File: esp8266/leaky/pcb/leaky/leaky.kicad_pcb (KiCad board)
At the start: 2 copper layers, 100 x 100 mm, 31 parts, among them J1 UART, J2 extra pins, Q1 BC327, SW1 sensing loop, U1 DD0405MA, U2 ESP-12F

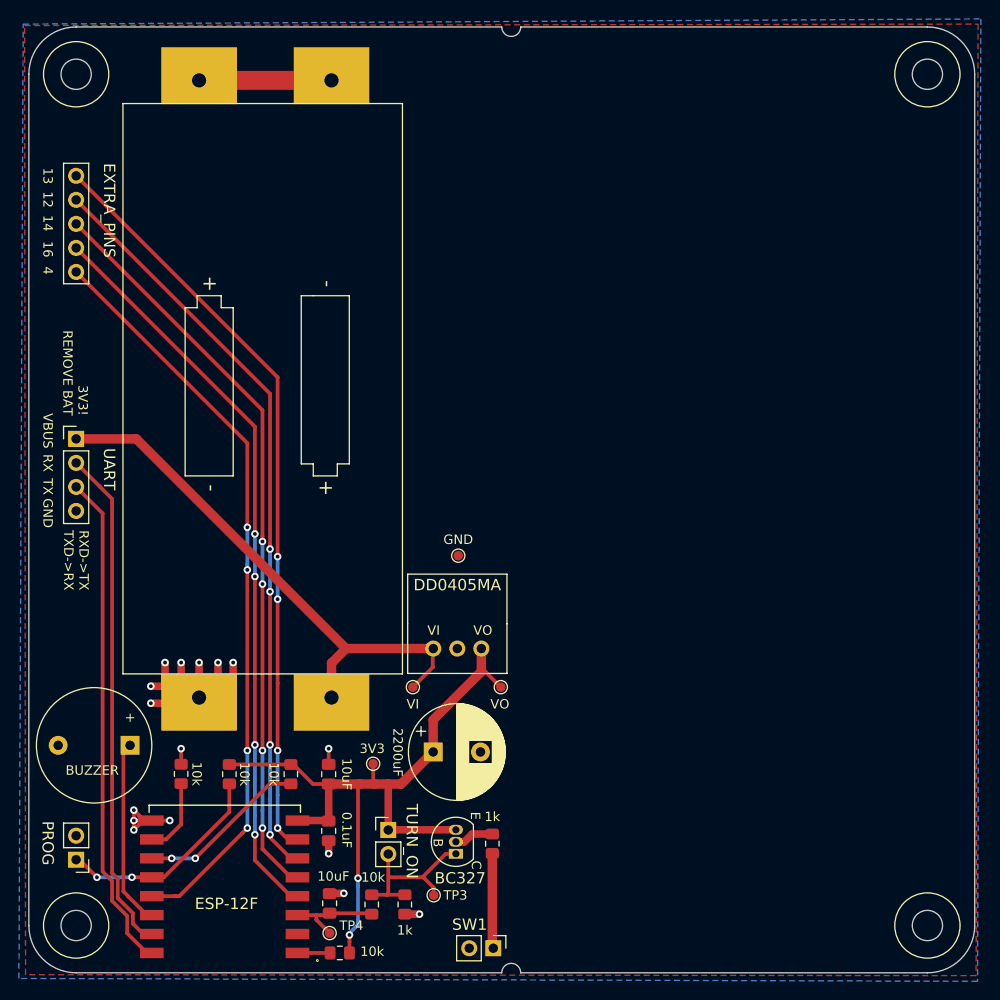
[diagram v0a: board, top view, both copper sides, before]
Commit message: leaky: Move TP4
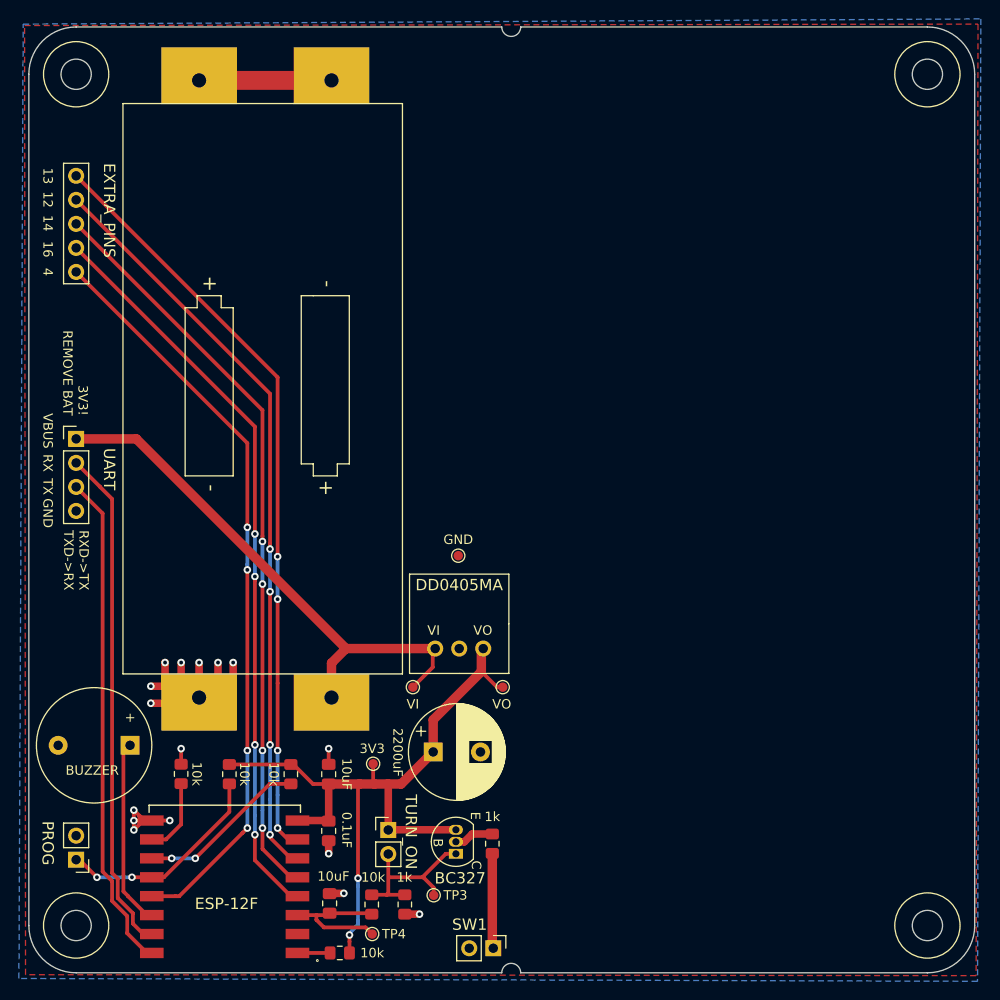
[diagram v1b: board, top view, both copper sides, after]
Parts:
- moved TP4 4.50 mm to (56.3, 115.9)
- moved U1 0.20 mm to (65.5, 78.1)
- moved TP6 0.20 mm to (70.1, 89.8)
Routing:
- net EN: track 11.2 -> 15.7 mm
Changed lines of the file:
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@@
     (thickness 1.6)
     (drawings 34)
-    (tracks 235)
+    (tracks 237)
     (zones 0)
     (modules 31)
@@
   )
   (setup
-    (last_trace_width 0.25)
+    (last_trace_width 0.4)
     (user_trace_width 0.4)
     (user_trace_width 1)
@@
   )
   (module _my:DD0405MA (layer F.Cu)
-    (at 65.3 78.1)
+    (at 65.5 78.1)
     (fp_text reference U1 (at 0 1.5) (layer F.Fab)
       (effects (font (size 1 1) (thickness 0.15)))
@@
       (effects (font (size 1 1) (thickness 0.15)))
     )
-    (fp_text value TURN_ON (at 2.5 1.2 270 unlocked) (layer F.SilkS)
+    (fp_text value TURN_ON (at 2.4 0.2 270 unlocked) (layer F.SilkS)
       (effects (font (size 1.2 1.2) (thickness 0.15)))
     )
@@
       (effects (font (size 1 1) (thickness 0.15)))
     )
-    (fp_text value 1k (at 2.725 0 180) (layer F.SilkS)
+    (fp_text value 1k (at -2.875 0.05 180) (layer F.SilkS)
       (effects (font (size 1 1) (thickness 0.15)))
     )
@@
       (effects (font (size 1 1) (thickness 0.15)))
     )
-    (fp_text value 10k (at 3.425 -0.15) (layer F.SilkS)
+    (fp_text value 10k (at 3.425 0) (layer F.SilkS)
       (effects (font (size 1 1) (thickness 0.15)))
     )
@@
   )
   (module TestPoint:TestPoint_Pad_D1.0mm (layer F.Cu)
-    (at 51.8 115.8)
+    (at 56.3 115.9)
     (descr "SMD pad as test Point, diameter 1.0mm")
     (tags "test point SMD pad")
     (attr virtual)
-    (fp_text reference TP4 (at 2.3 -0.8) (layer F.SilkS)
+    (fp_text reference TP4 (at 2.3 0) (layer F.SilkS)
       (effects (font (size 1 1) (thickness 0.15)))
     )
@@
   )
   (module TestPoint:TestPoint_Pad_D1.0mm (layer F.Cu)
-    (at 69.9 89.8)
+    (at 70.1 89.8)
     (descr "SMD pad as test Point, diameter 1.0mm")
     (tags "test point SMD pad")
@@
     (effects (font (size 1 1) (thickness 0.15)) (justify left))
   )
-  (gr_text VO (at 69.8 91.6) (layer F.SilkS)
+  (gr_text VO (at 70 91.6) (layer F.SilkS)
     (effects (font (size 1 1) (thickness 0.15)))
   )
@@
     (effects (font (size 1 1) (thickness 0.15)))
   )
-  (gr_text 4 (at 22 45.75 270) (layer F.SilkS)
+  (gr_text 4 (at 22 45.9 270) (layer F.SilkS)
     (effects (font (size 1 1) (thickness 0.15)))
   )
@@
   (segment (start 53.9 116) (end 53.9 116.7) (width 0.4) (layer F.Cu) (net 1))
   (segment (start 67.86 88.16) (end 67.84 88.16) (width 0.4) (layer F.Cu) (net 1))
-  (segment (start 68.26 88.16) (end 67.86 88.16) (width 0.4) (layer F.Cu) (net 1))
-  (segment (start 69.9 89.8) (end 68.26 88.16) (width 0.4) (layer F.Cu) (net 1))
+  (segment (start 67.86 88.16) (end 69.5 89.8) (width 0.4) (layer F.Cu) (net 1))
+  (segment (start 69.5 89.8) (end 70.1 89.8) (width 0.4) (layer F.Cu) (net 1))
   (via (at 31.100022 103.9) (size 0.8) (drill 0.4) (layers F.Cu B.Cu) (net 2))
   (segment (start 33.7 103.9) (end 31.100022 103.9) (width 0.4) (layer F.Cu) (net 2))
@@
   (segment (start 56.15 113.7) (end 56.25 113.8) (width 0.4) (layer F.Cu) (net 3))
   (segment (start 51.8 113.7) (end 56.15 113.7) (width 0.4) (layer F.Cu) (net 3))
-  (segment (start 50.4 114.4) (end 51.8 115.8) (width 0.4) (layer F.Cu) (net 3))
-  (segment (start 50.4 113.9) (end 50.4 114.4) (width 0.4) (layer F.Cu) (net 3))
   (segment (start 47.7 113.9) (end 50.4 113.9) (width 0.4) (layer F.Cu) (net 3))
   (segment (start 50.4 113.9) (end 51.6 113.9) (width 0.4) (layer F.Cu) (net 3))
+  (segment (start 50.4 114.4) (end 50.4 113.9) (width 0.4) (layer F.Cu) (net 3))
+  (segment (start 51.2 115.2) (end 50.4 114.4) (width 0.4) (layer F.Cu) (net 3))
+  (segment (start 55.599999 115.199999) (end 51.2 115.2) (width 0.4) (layer F.Cu) (net 3))
+  (segment (start 56.3 115.9) (end 55.599999 115.199999) (width 0.4) (layer F.Cu) (net 3))
   (segment (start 38 25.65) (end 52 25.65) (width 2) (layer F.Cu) (net 4))
   (segment (start 53.53 85.72) (end 62.76 85.72) (width 1) (layer F.Cu) (net 4))

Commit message: leaky: Add sense loop to top
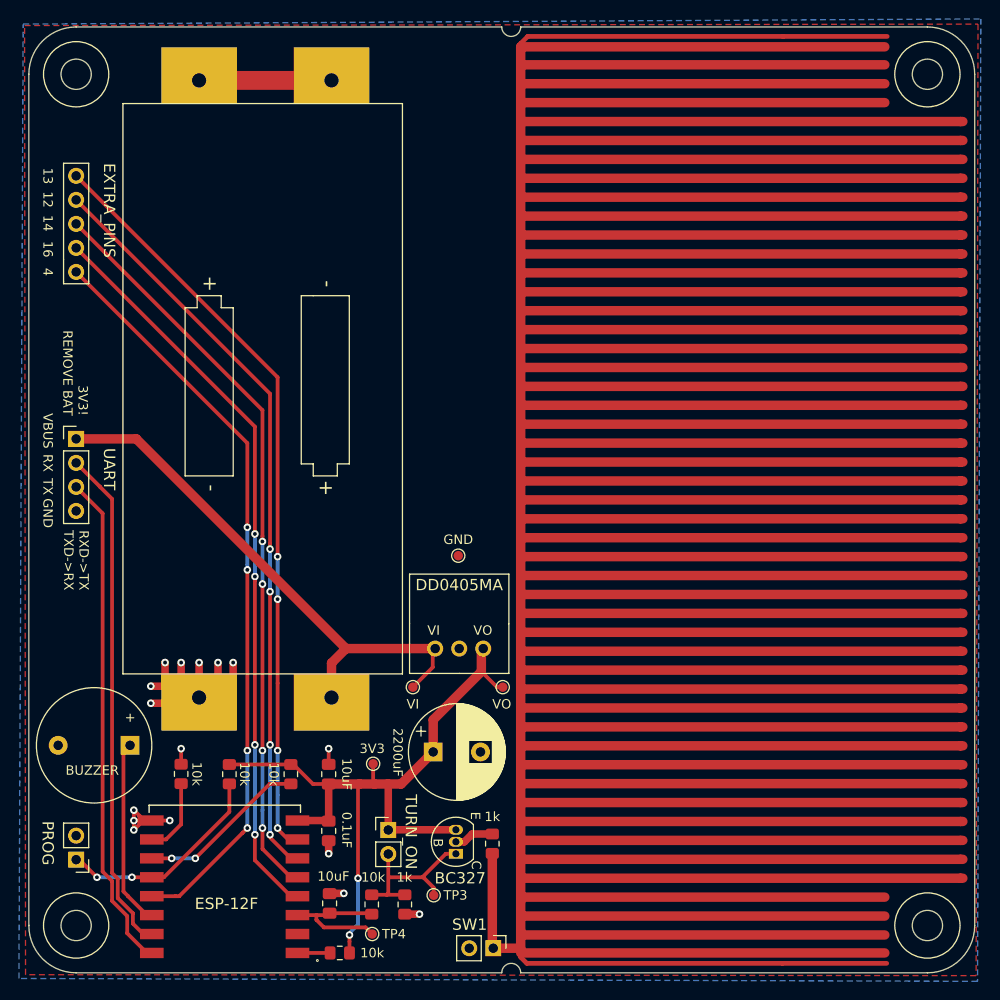
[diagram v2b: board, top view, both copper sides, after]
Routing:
- net Net-(R1-Pad2): track 10.1 -> 2411.8 mm
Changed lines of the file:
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@@
     (thickness 1.6)
     (drawings 34)
-    (tracks 237)
+    (tracks 342)
     (zones 0)
     (modules 31)
@@
     (37 F.SilkS user)
     (38 B.Mask user)
-    (39 F.Mask user)
+    (39 F.Mask user hide)
     (40 Dwgs.User user)
     (41 Cmts.User user)
@@
     (43 Eco2.User user)
     (44 Edge.Cuts user)
-    (45 Margin user)
+    (45 Margin user hide)
     (46 B.CrtYd user hide)
     (47 F.CrtYd user hide)
@@
   )
   (setup
-    (last_trace_width 0.4)
+    (last_trace_width 0.5)
     (user_trace_width 0.4)
+    (user_trace_width 0.5)
     (user_trace_width 1)
     (user_trace_width 2)
@@
     (effects (font (size 1 1) (thickness 0.15)) (justify right))
   )
-  (gr_poly (pts (xy 111.2 119.3) (xy 71 119.3) (xy 71 20.7) (xy 111.2 20.7)) (layer F.Mask) (width 0.1))
+  (gr_poly (pts (xy 111.2 119.5) (xy 71 119.5) (xy 71 20.5) (xy 111.2 20.5)) (layer F.Mask) (width 0.1))
   (gr_line (start 20 115) (end 20 25) (layer Edge.Cuts) (width 0.05))
   (gr_line (start 120 25) (end 120 115) (layer Edge.Cuts) (width 0.05))
@@
   (segment (start 69 117.3) (end 69.1 117.4) (width 1) (layer F.Cu) (net 20))
   (segment (start 69 107.375) (end 69 117.3) (width 1) (layer F.Cu) (net 20))
+  (segment (start 69.1 117.4) (end 72 117.4) (width 1) (layer F.Cu) (net 20))
+  (segment (start 72 117.9) (end 110.5 117.9) (width 1) (layer F.Cu) (net 20))
+  (segment (start 72 117.4) (end 72 116) (width 1) (layer F.Cu) (net 20))
+  (segment (start 72 116) (end 110.5 116) (width 1) (layer F.Cu) (net 20))
+  (segment (start 72 116) (end 72 115.5) (width 1) (layer F.Cu) (net 20))
+  (segment (start 72 115.5) (end 72 114) (width 1) (layer F.Cu) (net 20))
+  (segment (start 72 114) (end 72 112.5) (width 1) (layer F.Cu) (net 20))
+  (segment (start 72 114) (end 110.5 114) (width 1) (layer F.Cu) (net 20))
+  (segment (start 72 112) (end 110.5 112) (width 1) (layer F.Cu) (net 20))
+  (segment (start 72 110) (end 118.5 110) (width 1) (layer F.Cu) (net 20))
+  (segment (start 72 112.5) (end 72 110) (width 1) (layer F.Cu) (net 20))
+  (segment (start 118.75 110) (end 118.5 110) (width 1) (layer F.Cu) (net 20))
+  (segment (start 118.75 108) (end 118.5 108) (width 1) (layer F.Cu) (net 20))
+  (segment (start 72 108) (end 118.5 108) (width 1) (layer F.Cu) (net 20))
+  (segment (start 72 106) (end 118.5 106) (width 1) (layer F.Cu) (net 20))
+  (segment (start 118.75 106) (end 118.5 106) (width 1) (layer F.Cu) (net 20))
+  (segment (start 72 104) (end 118.5 104) (width 1) (layer F.Cu) (net 20))
+  (segment (start 118.75 104) (end 118.5 104) (width 1) (layer F.Cu) (net 20))
+  (segment (start 72 102) (end 118.5 102) (width 1) (layer F.Cu) (net 20))
+  (segment (start 118.75 102) (end 118.5 102) (width 1) (layer F.Cu) (net 20))
+  (segment (start 118.75 100) (end 118.5 100) (width 1) (layer F.Cu) (net 20))
+  (segment (start 72 100) (end 118.5 100) (width 1) (layer F.Cu) (net 20))
+  (segment (start 72 98) (end 118.5 98) (width 1) (layer F.Cu) (net 20))
+  (segment (start 118.75 98) (end 118.5 98) (width 1) (layer F.Cu) (net 20))
+  (segment (start 118.75 96) (end 118.5 96) (width 1) (layer F.Cu) (net 20))
+  (segment (start 72 96) (end 118.5 96) (width 1) (layer F.Cu) (net 20))
+  (segment (start 118.75 94) (end 118.5 94) (width 1) (layer F.Cu) (net 20))
+  (segment (start 72 94) (end 118.5 94) (width 1) (layer F.Cu) (net 20))
+  (segment (start 118.75 92) (end 118.5 92) (width 1) (layer F.Cu) (net 20))
+  (segment (start 72 92) (end 118.5 92) (width 1) (layer F.Cu) (net 20))
+  (segment (start 118.75 90) (end 118.5 90) (width 1) (layer F.Cu) (net 20))
+  (segment (start 72 90) (end 118.5 90) (width 1) (layer F.Cu) (net 20))
+  (segment (start 118.75 88) (end 118.5 88) (width 1) (layer F.Cu) (net 20))
+  (segment (start 72 88) (end 118.5 88) (width 1) (layer F.Cu) (net 20))
+  (segment (start 118.75 86) (end 118.5 86) (width 1) (layer F.Cu) (net 20))
+  (segment (start 72 86) (end 118.5 86) (width 1) (layer F.Cu) (net 20))
+  (segment (start 118.75 84) (end 118.5 84) (width 1) (layer F.Cu) (net 20))
+  (segment (start 72 84) (end 118.5 84) (width 1) (layer F.Cu) (net 20))
+  (segment (start 118.75 82) (end 118.5 82) (width 1) (layer F.Cu) (net 20))
+  (segment (start 72 82) (end 118.5 82) (width 1) (layer F.Cu) (net 20))
+  (segment (start 118.75 80) (end 118.5 80) (width 1) (layer F.Cu) (net 20))
+  (segment (start 72 80) (end 118.5 80) (width 1) (layer F.Cu) (net 20))
+  (segment (start 72 78) (end 118.5 78) (width 1) (layer F.Cu) (net 20))
+  (segment (start 118.75 78) (end 118.5 78) (width 1) (layer F.Cu) (net 20))
+  (segment (start 72 76) (end 118.5 76) (width 1) (layer F.Cu) (net 20))
+  (segment (start 118.75 76) (end 118.5 76) (width 1) (layer F.Cu) (net 20))
+  (segment (start 118.75 72) (end 118.5 72) (width 1) (layer F.Cu) (net 20))
+  (segment (start 118.75 70) (end 118.5 70) (width 1) (layer F.Cu) (net 20))
+  (segment (start 72 74) (end 118.5 74) (width 1) (layer F.Cu) (net 20))
+  (segment (start 118.75 74) (end 118.5 74) (width 1) (layer F.Cu) (net 20))
+  (segment (start 72 72) (end 118.5 72) (width 1) (layer F.Cu) (net 20))
+  (segment (start 72 70) (end 118.5 70) (width 1) (layer F.Cu) (net 20))
+  (segment (start 118.75 62) (end 118.5 62) (width 1) (layer F.Cu) (net 20))
+  (segment (start 72 66) (end 118.5 66) (width 1) (layer F.Cu) (net 20))
+  (segment (start 118.75 66) (end 118.5 66) (width 1) (layer F.Cu) (net 20))
+  (segment (start 72 64) (end 118.5 64) (width 1) (layer F.Cu) (net 20))
+  (segment (start 72 62) (end 118.5 62) (width 1) (layer F.Cu) (net 20))
+  (segment (start 72 68) (end 118.5 68) (width 1) (layer F.Cu) (net 20))
+  (segment (start 118.75 64) (end 118.5 64) (width 1) (layer F.Cu) (net 20))
+  (segment (start 118.75 68) (end 118.5 68) (width 1) (layer F.Cu) (net 20))
+  (segment (start 118.75 54) (end 118.5 54) (width 1) (layer F.Cu) (net 20))
+  (segment (start 72 58) (end 118.5 58) (width 1) (layer F.Cu) (net 20))
+  (segment (start 72 56) (end 118.5 56) (width 1) (layer F.Cu) (net 20))
+  (segment (start 118.75 60) (end 118.5 60) (width 1) (layer F.Cu) (net 20))
+  (segment (start 118.75 56) (end 118.5 56) (width 1) (layer F.Cu) (net 20))
+  (segment (start 118.75 58) (end 118.5 58) (width 1) (layer F.Cu) (net 20))
+  (segment (start 72 54) (end 118.5 54) (width 1) (layer F.Cu) (net 20))
+  (segment (start 72 60) (end 118.5 60) (width 1) (layer F.Cu) (net 20))
+  (segment (start 118.75 46) (end 118.5 46) (width 1) (layer F.Cu) (net 20))
+  (segment (start 72 50) (end 118.5 50) (width 1) (layer F.Cu) (net 20))
+  (segment (start 72 48) (end 118.5 48) (width 1) (layer F.Cu) (net 20))
+  (segment (start 118.75 52) (end 118.5 52) (width 1) (layer F.Cu) (net 20))
+  (segment (start 118.75 48) (end 118.5 48) (width 1) (layer F.Cu) (net 20))
+  (segment (start 118.75 50) (end 118.5 50) (width 1) (layer F.Cu) (net 20))
+  (segment (start 72 46) (end 118.5 46) (width 1) (layer F.Cu) (net 20))
+  (segment (start 72 52) (end 118.5 52) (width 1) (layer F.Cu) (net 20))
+  (segment (start 118.75 42) (end 118.5 42) (width 1) (layer F.Cu) (net 20))
+  (segment (start 72 44) (end 118.5 44) (width 1) (layer F.Cu) (net 20))
+  (segment (start 72 38) (end 118.5 38) (width 1) (layer F.Cu) (net 20))
+  (segment (start 118.75 38) (end 118.5 38) (width 1) (layer F.Cu) (net 20))
+  (segment (start 72 40) (end 118.5 40) (width 1) (layer F.Cu) (net 20))
+  (segment (start 72 42) (end 118.5 42) (width 1) (layer F.Cu) (net 20))
+  (segment (start 118.75 40) (end 118.5 40) (width 1) (layer F.Cu) (net 20))
+  (segment (start 118.75 44) (end 118.5 44) (width 1) (layer F.Cu) (net 20))
+  (segment (start 118.75 34) (end 118.5 34) (width 1) (layer F.Cu) (net 20))
+  (segment (start 72 30) (end 118.5 30) (width 1) (layer F.Cu) (net 20))
+  (segment (start 118.75 30) (end 118.5 30) (width 1) (layer F.Cu) (net 20))
+  (segment (start 118.75 32) (end 118.5 32) (width 1) (layer F.Cu) (net 20))
+  (segment (start 72 36) (end 118.5 36) (width 1) (layer F.Cu) (net 20))
+  (segment (start 72 34) (end 118.5 34) (width 1) (layer F.Cu) (net 20))
+  (segment (start 118.75 36) (end 118.5 36) (width 1) (layer F.Cu) (net 20))
+  (segment (start 72 32) (end 118.5 32) (width 1) (layer F.Cu) (net 20))
+  (segment (start 72 28) (end 110.5 28) (width 1) (layer F.Cu) (net 20))
+  (segment (start 110.5 26) (end 72 26) (width 1) (layer F.Cu) (net 20))
+  (segment (start 110.5 22.1) (end 72 22.1) (width 1) (layer F.Cu) (net 20))
+  (segment (start 110.5 24) (end 72 24) (width 1) (layer F.Cu) (net 20))
+  (segment (start 72 22.1) (end 72 110) (width 1) (layer F.Cu) (net 20))
+  (segment (start 72 22.1) (end 72 21.75) (width 0.5) (layer F.Cu) (net 20))
+  (segment (start 72 21.75) (end 72.75 21) (width 0.5) (layer F.Cu) (net 20))
+  (segment (start 72.75 21) (end 99.75 21) (width 0.5) (layer F.Cu) (net 20))
+  (segment (start 99.75 21) (end 110.75 21) (width 0.5) (layer F.Cu) (net 20))
+  (segment (start 99.7 119) (end 110.7 119) (width 0.5) (layer F.Cu) (net 20))
+  (segment (start 72.65 119) (end 99.65 119) (width 0.5) (layer F.Cu) (net 20))
+  (segment (start 72 118.35) (end 72.65 119) (width 0.5) (layer F.Cu) (net 20))
+  (segment (start 72 117.9) (end 72 118.35) (width 0.5) (layer F.Cu) (net 20))
   (zone (net 2) (net_name GND) (layer B.Cu) (hatch edge 0.508)
     (connect_pads (clearance 0.508))
